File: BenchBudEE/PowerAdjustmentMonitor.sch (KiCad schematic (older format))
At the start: 15 parts

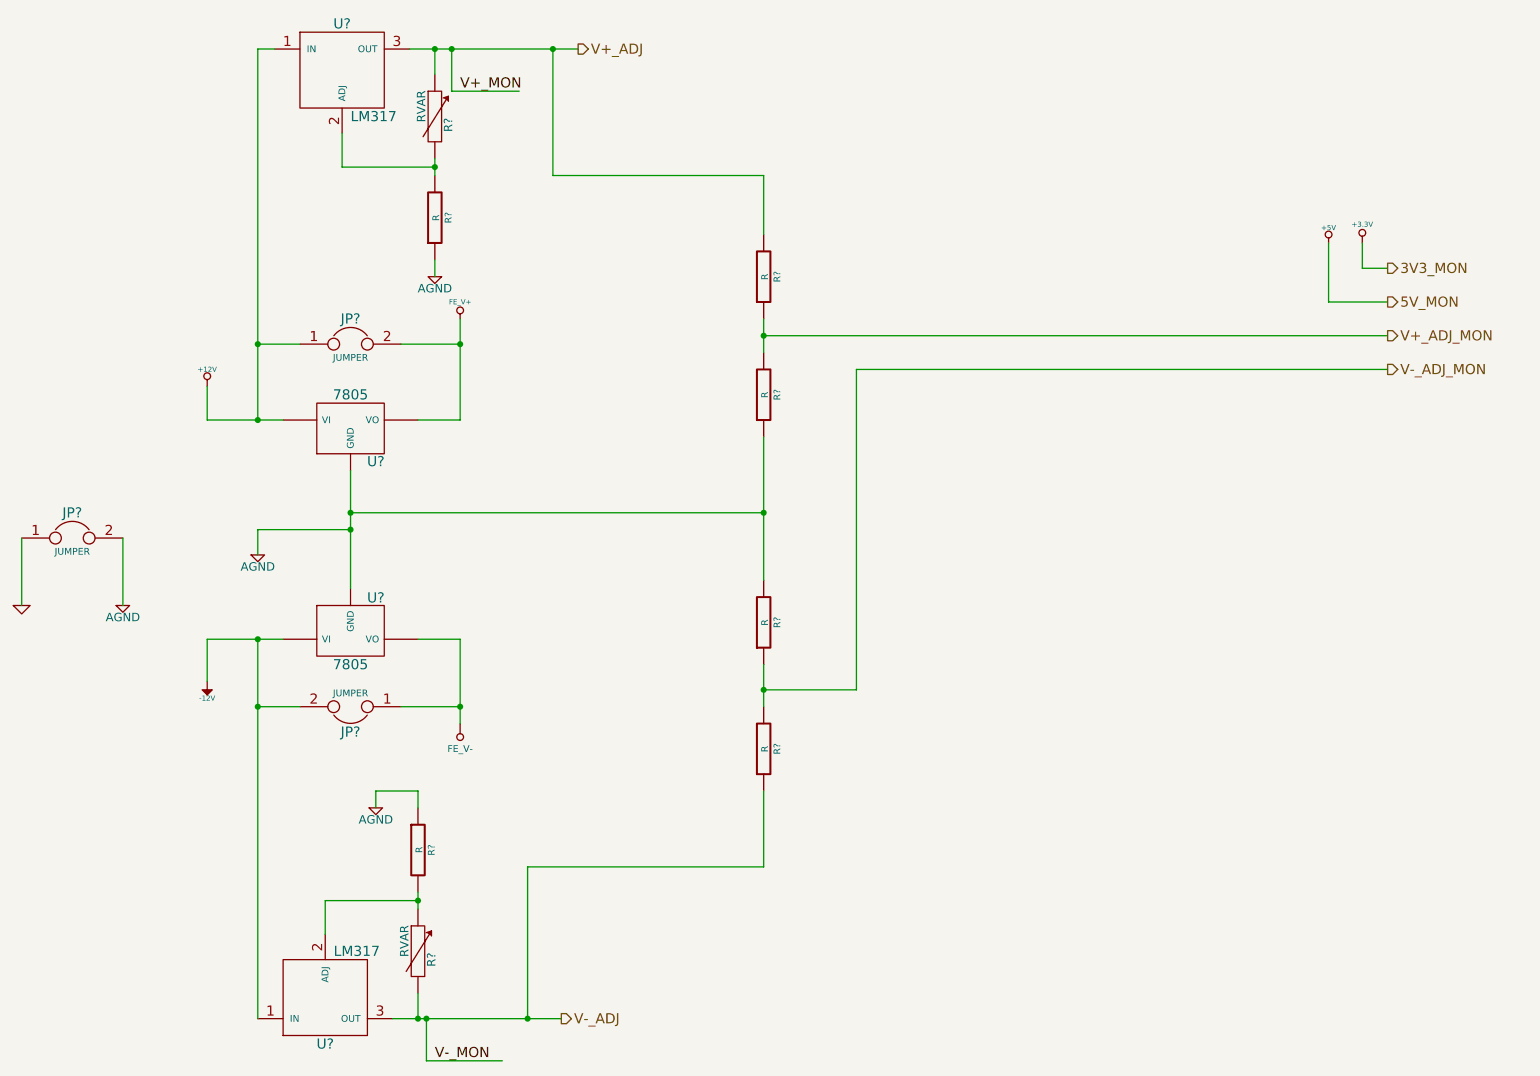
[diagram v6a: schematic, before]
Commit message: Associating and Placing the Relay Module
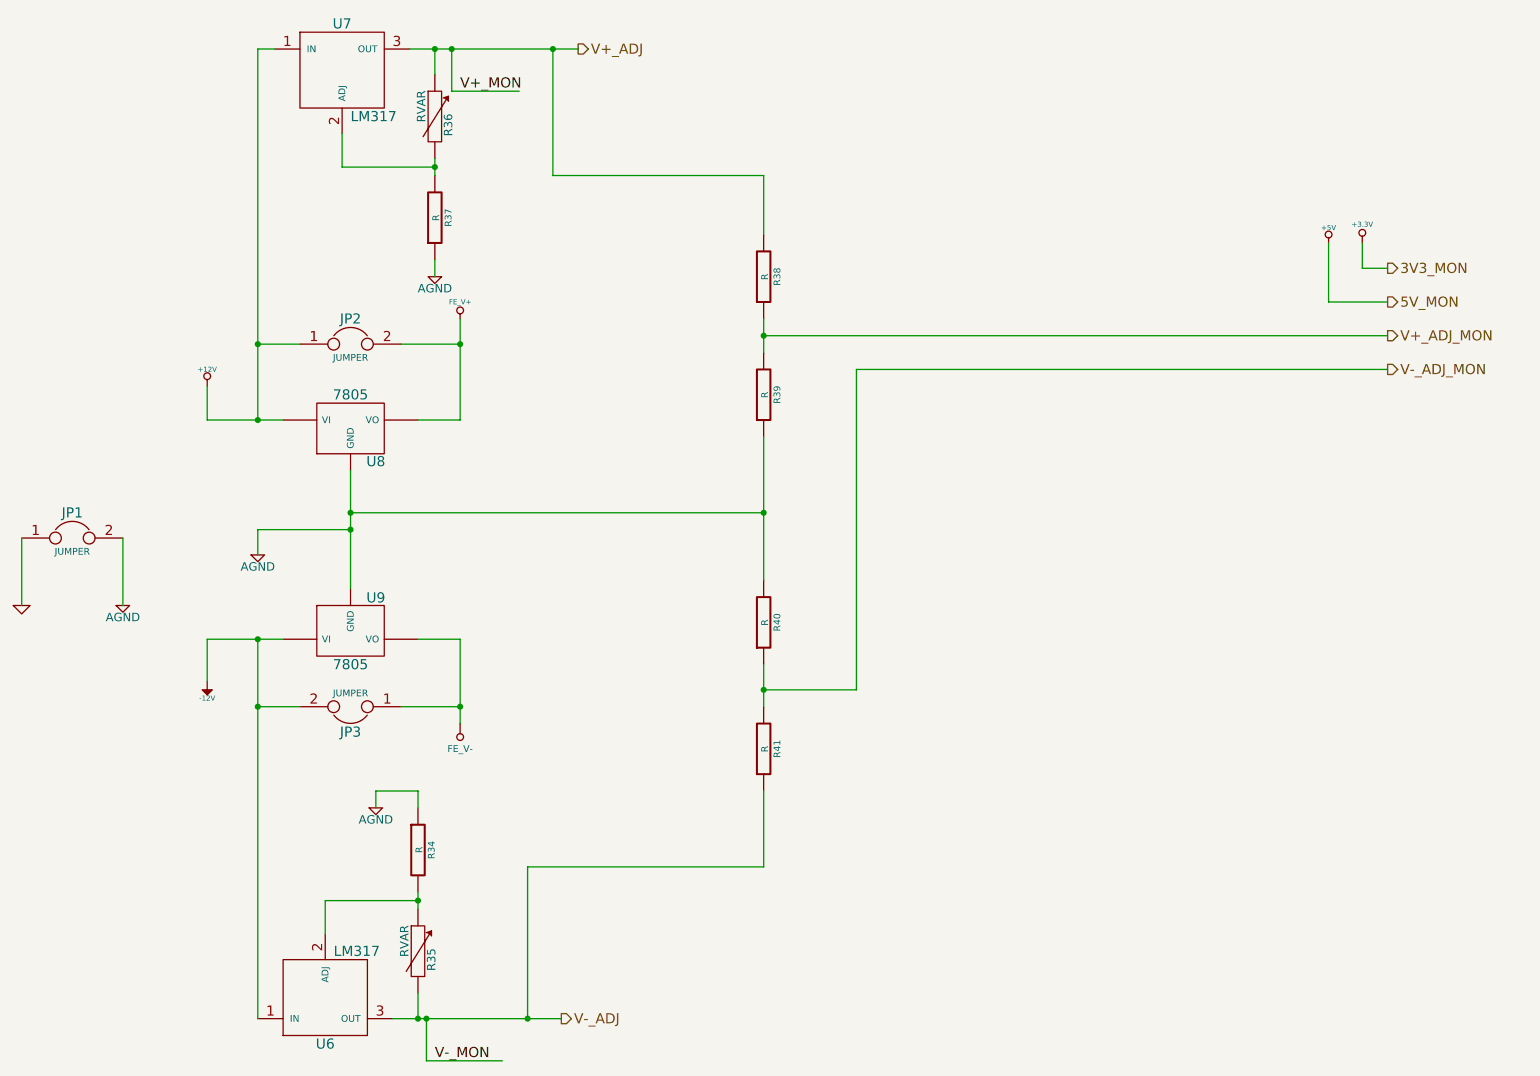
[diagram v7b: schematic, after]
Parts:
- gave numbers to parts that had none: 15
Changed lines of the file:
@@
 $EndDescr
 $Comp
-L +3.3V #PWR038
+L +3.3V #PWR50
 U 1 1 52F67086
 P 8800 2050
-F 0 "#PWR038" H 8800 2010 30  0001 C CNN
+F 0 "#PWR50" H 8800 2010 30  0001 C CNN
 F 1 "+3.3V" H 8800 2160 30  0000 C CNN
 F 2 "" H 8800 2050 60  0000 C CNN
@@
 $EndComp
 $Comp
-L +5V #PWR039
+L +5V #PWR49
 U 1 1 52F6708C
 P 8600 2050
-F 0 "#PWR039" H 8600 2140 20  0001 C CNN
+F 0 "#PWR49" H 8600 2140 20  0001 C CNN
 F 1 "+5V" H 8600 2140 30  0000 C CNN
 F 2 "" H 8600 2050 60  0000 C CNN
@@
 $EndComp
 $Comp
-L +12V #PWR040
+L +12V #PWR42
 U 1 1 52F67112
 P 1950 2900
-F 0 "#PWR040" H 1950 2850 20  0001 C CNN
+F 0 "#PWR42" H 1950 2850 20  0001 C CNN
 F 1 "+12V" H 1950 3000 30  0000 C CNN
 F 2 "" H 1950 2900 60  0000 C CNN
@@
 $EndComp
 $Comp
-L -12V #PWR041
+L -12V #PWR43
 U 1 1 52F67118
 P 1950 4650
-F 0 "#PWR041" H 1950 4780 20  0001 C CNN
+F 0 "#PWR43" H 1950 4780 20  0001 C CNN
 F 1 "-12V" H 1950 4750 30  0000 C CNN
 F 2 "" H 1950 4650 60  0000 C CNN
@@
 $EndComp
 $Comp
-L LM317 U?
+L LM317 U6
 U 1 1 52F6715F
 P 2650 6500
-F 0 "U?" H 2650 6800 60  0000 C CNN
+F 0 "U6" H 2650 6800 60  0000 C CNN
 F 1 "LM317" H 2700 6250 60  0000 L CNN
 F 2 "~" H 2650 6500 60  0000 C CNN
@@
 $EndComp
 $Comp
-L JUMPER JP?
+L JUMPER JP2
 U 1 1 52F6717A
 P 2800 2650
-F 0 "JP?" H 2800 2800 60  0000 C CNN
+F 0 "JP2" H 2800 2800 60  0000 C CNN
 F 1 "JUMPER" H 2800 2570 40  0000 C CNN
 F 2 "~" H 2800 2650 60  0000 C CNN
@@
 $EndComp
 $Comp
-L JUMPER JP?
+L JUMPER JP3
 U 1 1 52F67191
 P 2800 4800
-F 0 "JP?" H 2800 4950 60  0000 C CNN
+F 0 "JP3" H 2800 4950 60  0000 C CNN
 F 1 "JUMPER" H 2800 4720 40  0000 C CNN
 F 2 "~" H 2800 4800 60  0000 C CNN
@@
 $EndComp
 $Comp
-L AGND #PWR042
+L AGND #PWR44
 U 1 1 52F671D9
 P 2250 3900
-F 0 "#PWR042" H 2250 3900 40  0001 C CNN
+F 0 "#PWR44" H 2250 3900 40  0001 C CNN
 F 1 "AGND" H 2250 3830 50  0000 C CNN
 F 2 "" H 2250 3900 60  0000 C CNN
@@
 $EndComp
 $Comp
-L AGND #PWR043
+L AGND #PWR41
 U 1 1 52F671E6
 P 1450 4200
-F 0 "#PWR043" H 1450 4200 40  0001 C CNN
+F 0 "#PWR41" H 1450 4200 40  0001 C CNN
 F 1 "AGND" H 1450 4130 50  0000 C CNN
 F 2 "" H 1450 4200 60  0000 C CNN
@@
 $EndComp
 $Comp
-L GND #PWR044
+L GND #PWR40
 U 1 1 52F671EC
 P 850 4200
-F 0 "#PWR044" H 850 4200 30  0001 C CNN
+F 0 "#PWR40" H 850 4200 30  0001 C CNN
 F 1 "GND" H 850 4130 30  0001 C CNN
 F 2 "" H 850 4200 60  0000 C CNN
@@
 $EndComp
 $Comp
-L JUMPER JP?
+L JUMPER JP1
 U 1 1 52F671F2
 P 1150 3800
-F 0 "JP?" H 1150 3950 60  0000 C CNN
+F 0 "JP1" H 1150 3950 60  0000 C CNN
 F 1 "JUMPER" H 1150 3720 40  0000 C CNN
 F 2 "~" H 1150 3800 60  0000 C CNN
@@
 $EndComp
 $Comp
-L FE_V+ #PWR045
+L FE_V+ #PWR47
 U 1 1 52F672AE
 P 3450 2500
-F 0 "#PWR045" H 3450 2600 30  0001 C CNN
+F 0 "#PWR47" H 3450 2600 30  0001 C CNN
 F 1 "FE_V+" H 3450 2600 30  0000 C CNN
 F 2 "" H 3450 2500 60  0000 C CNN
@@
 $EndComp
 $Comp
-L FE_V- #PWR?
+L FE_V- #PWR48
 U 1 1 52F672D7
 P 3450 4900
-F 0 "#PWR?" H 3450 5100 40  0001 C CNN
+F 0 "#PWR48" H 3450 5100 40  0001 C CNN
 F 1 "FE_V-" H 3450 5050 40  0000 C CNN
 F 2 "" H 3450 4900 60  0000 C CNN
@@
 $EndComp
 $Comp
-L 7805 U?
+L 7805 U8
 U 1 1 52F67504
 P 2800 3150
-F 0 "U?" H 2950 2954 60  0000 C CNN
+F 0 "U8" H 2950 2954 60  0000 C CNN
 F 1 "7805" H 2800 3350 60  0000 C CNN
 F 2 "~" H 2800 3150 60  0000 C CNN
@@
 $EndComp
 $Comp
-L 7805 U?
+L 7805 U9
 U 1 1 52F67511
 P 2800 4350
-F 0 "U?" H 2950 4154 60  0000 C CNN
+F 0 "U9" H 2950 4154 60  0000 C CNN
 F 1 "7805" H 2800 4550 60  0000 C CNN
 F 2 "~" H 2800 4350 60  0000 C CNN
@@
 $EndComp
 $Comp
-L R R?
+L R R34
 U 1 1 52F67578
 P 3200 5650
-F 0 "R?" V 3280 5650 40  0000 C CNN
+F 0 "R34" V 3280 5650 40  0000 C CNN
 F 1 "R" V 3207 5651 40  0000 C CNN
 F 2 "~" V 3130 5650 30  0000 C CNN
@@
 $EndComp
 $Comp
-L AGND #PWR046
+L AGND #PWR45
 U 1 1 52F67601
 P 2950 5400
-F 0 "#PWR046" H 2950 5400 40  0001 C CNN
+F 0 "#PWR45" H 2950 5400 40  0001 C CNN
 F 1 "AGND" H 2950 5330 50  0000 C CNN
 F 2 "" H 2950 5400 60  0000 C CNN
@@
 $EndComp
 $Comp
-L LM317 U?
+L LM317 U7
 U 1 1 52F67627
 P 2750 1050
-F 0 "U?" H 2750 1350 60  0000 C CNN
+F 0 "U7" H 2750 1350 60  0000 C CNN
 F 1 "LM317" H 2800 800 60  0000 L CNN
 F 2 "~" H 2750 1050 60  0000 C CNN
@@
 $EndComp
 $Comp
-L R R?
+L R R37
 U 1 1 52F6762E
 P 3300 1900
-F 0 "R?" V 3380 1900 40  0000 C CNN
+F 0 "R37" V 3380 1900 40  0000 C CNN
 F 1 "R" V 3307 1901 40  0000 C CNN
 F 2 "~" V 3230 1900 30  0000 C CNN
@@
 $EndComp
 $Comp
-L AGND #PWR047
+L AGND #PWR46
 U 1 1 52F67640
 P 3300 2250
-F 0 "#PWR047" H 3300 2250 40  0001 C CNN
+F 0 "#PWR46" H 3300 2250 40  0001 C CNN
 F 1 "AGND" H 3300 2180 50  0000 C CNN
 F 2 "" H 3300 2250 60  0000 C CNN
@@
 V-_ADJ_MON
 $Comp
-L R R?
+L R R38
 U 1 1 52F74407
 P 5250 2250
-F 0 "R?" V 5330 2250 40  0000 C CNN
+F 0 "R38" V 5330 2250 40  0000 C CNN
 F 1 "R" V 5257 2251 40  0000 C CNN
 F 2 "~" V 5180 2250 30  0000 C CNN
@@
 $EndComp
 $Comp
-L R R?
+L R R39
 U 1 1 52F7440D
 P 5250 2950
-F 0 "R?" V 5330 2950 40  0000 C CNN
+F 0 "R39" V 5330 2950 40  0000 C CNN
 F 1 "R" V 5257 2951 40  0000 C CNN
 F 2 "~" V 5180 2950 30  0000 C CNN
@@
 Connection ~ 2800 3650
 $Comp
-L R R?
+L R R40
 U 1 1 52F744AD
 P 5250 4300
-F 0 "R?" V 5330 4300 40  0000 C CNN
+F 0 "R40" V 5330 4300 40  0000 C CNN
 F 1 "R" V 5257 4301 40  0000 C CNN
 F 2 "~" V 5180 4300 30  0000 C CNN
@@
 $EndComp
 $Comp
-L R R?
+L R R41
 U 1 1 52F744B3
 P 5250 5050
-F 0 "R?" V 5330 5050 40  0000 C CNN
+F 0 "R41" V 5330 5050 40  0000 C CNN
 F 1 "R" V 5257 5051 40  0000 C CNN
 F 2 "~" V 5180 5050 30  0000 C CNN
@@
 	5800 2800 8950 2800
 $Comp
-L RVAR R?
+L RVAR R35
 U 1 1 52F7542C
 P 3200 6250
-F 0 "R?" V 3280 6200 50  0000 C CNN
+F 0 "R35" V 3280 6200 50  0000 C CNN
 F 1 "RVAR" V 3120 6310 50  0000 C CNN
 F 2 "~" H 3200 6250 60  0000 C CNN
@@
 $EndComp
 $Comp
-L RVAR R?
+L RVAR R36
 U 1 1 52F75439
 P 3300 1300
-F 0 "R?" V 3380 1250 50  0000 C CNN
+F 0 "R36" V 3380 1250 50  0000 C CNN
 F 1 "RVAR" V 3220 1360 50  0000 C CNN
 F 2 "~" H 3300 1300 60  0000 C CNN
